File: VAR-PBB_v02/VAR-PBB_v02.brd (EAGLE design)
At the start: 83.5 x 86.4 mm, 32 parts, among them J1 ANDERSON_POWER_POLE, J11 CON1X2_SHROUDED, J2 ANDERSON_POWER_POLE, J3 CON1X2_SHROUDED, J4 CON1X2_SHROUDED, J5 CON1X2_SHROUDED, J6 CON1X2_SHROUDED, J7 CON1X2_SHROUDED, J8 CON1X2_SHROUDED, U1 OKI-78SR, U2 XL6009, U3 XL6009, U4 XL6009, U5 LP2985AIM5-1.5, U6 TPS259271DRCR

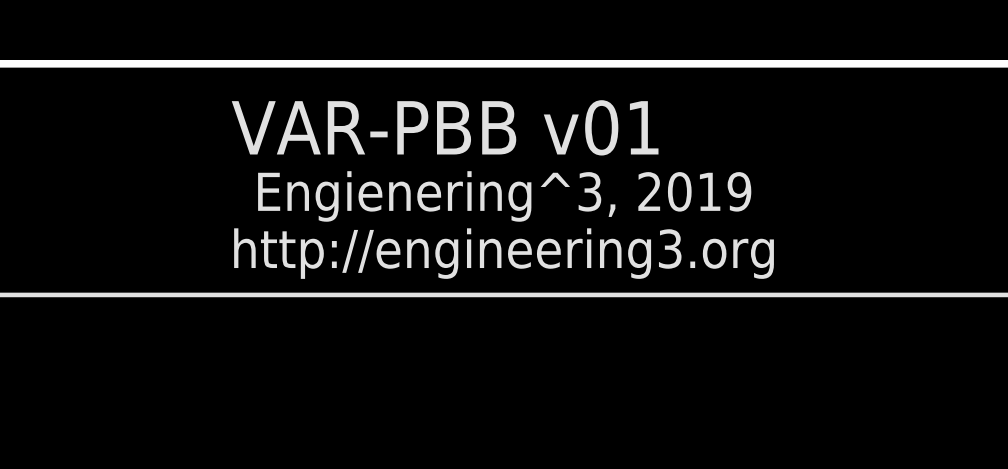
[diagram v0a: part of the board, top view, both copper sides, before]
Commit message: Fixed misspelled top silk text "Engineering" to create v2.0 design.
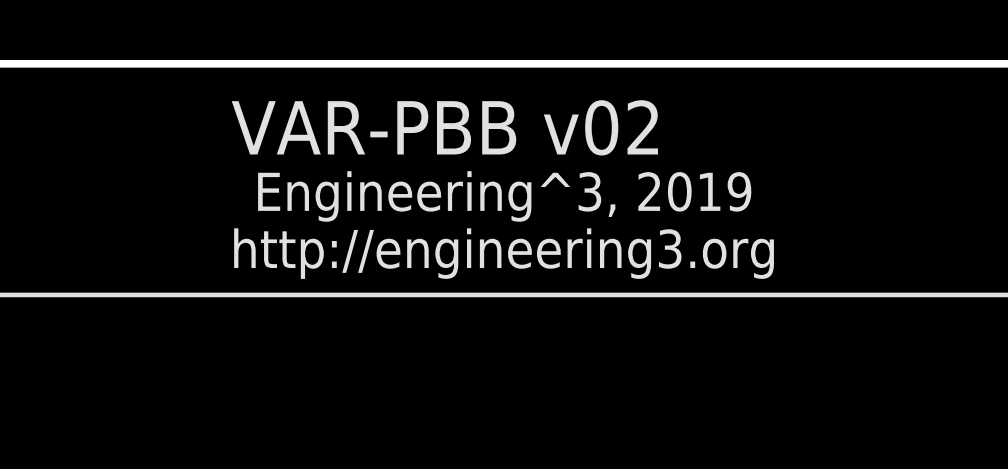
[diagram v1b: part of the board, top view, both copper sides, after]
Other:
- board text added: "Engineering^3, 2019 http://engineering3.org"
- board text added: "VAR-PBB v02"
- board text removed: "Engienering^3, 2019 http://engineering3.org"
- board text removed: "VAR-PBB v01"
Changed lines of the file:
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@@
 <?xml version="1.0" encoding="utf-8"?>
 <!DOCTYPE eagle SYSTEM "eagle.dtd">
-<eagle version="9.5.2">
+<eagle version="9.6.2">
 <drawing>
 <settings>
@@
 <text x="76.2" y="19.05" size="1.778" layer="21" font="vector" ratio="12" rot="R90">ON</text>
 <text x="75.946" y="31.75" size="1.778" layer="21" font="vector" ratio="12" rot="R90">OFF</text>
-<text x="30.4546" y="83.3374" size="1.778" layer="21" font="vector" ratio="12">VAR-PBB v01</text>
+<text x="30.4546" y="83.3374" size="1.778" layer="21" font="vector" ratio="12">VAR-PBB v02</text>
 <text x="34.0614" y="50.9778" size="1.27" layer="21" font="vector" ratio="18">J1</text>
 <hole x="51.308" y="38.354" drill="3.2"/>
 <hole x="27.686" y="38.354" drill="3.2"/>
-<text x="39.5478" y="79.5528" size="1.27" layer="21" font="vector" ratio="12" align="bottom-center">Engienering^3, 2019
+<text x="39.5478" y="79.5528" size="1.27" layer="21" font="vector" ratio="12" align="bottom-center">Engineering^3, 2019
 http://engineering3.org</text>
 <text x="35.2552" y="7.9756" size="1.778" layer="22" rot="MR180">RoSH
